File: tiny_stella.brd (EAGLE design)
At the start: 99.7 x 85.1 mm, 84 parts, among them IC1 74LS00D, SW1 RGT_DIFFICULTY, SW2 LFT_DIFFICULTY, SW3 ON/OFF, SW4 ON/OFF, T1 2N3904, T2 PN3906, T3 PN3906, T4 PN3906, X1 SSW-112-02-G-Q

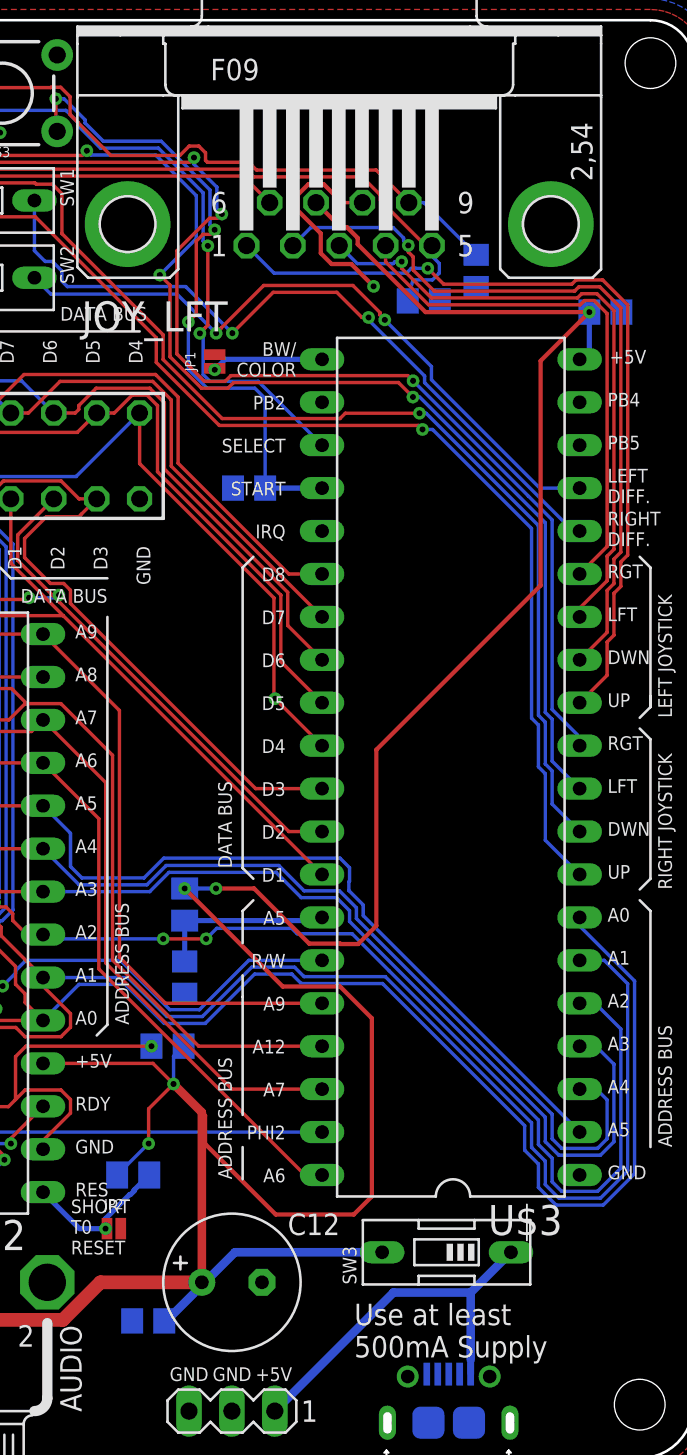
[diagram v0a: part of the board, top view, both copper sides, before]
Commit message: added monogram
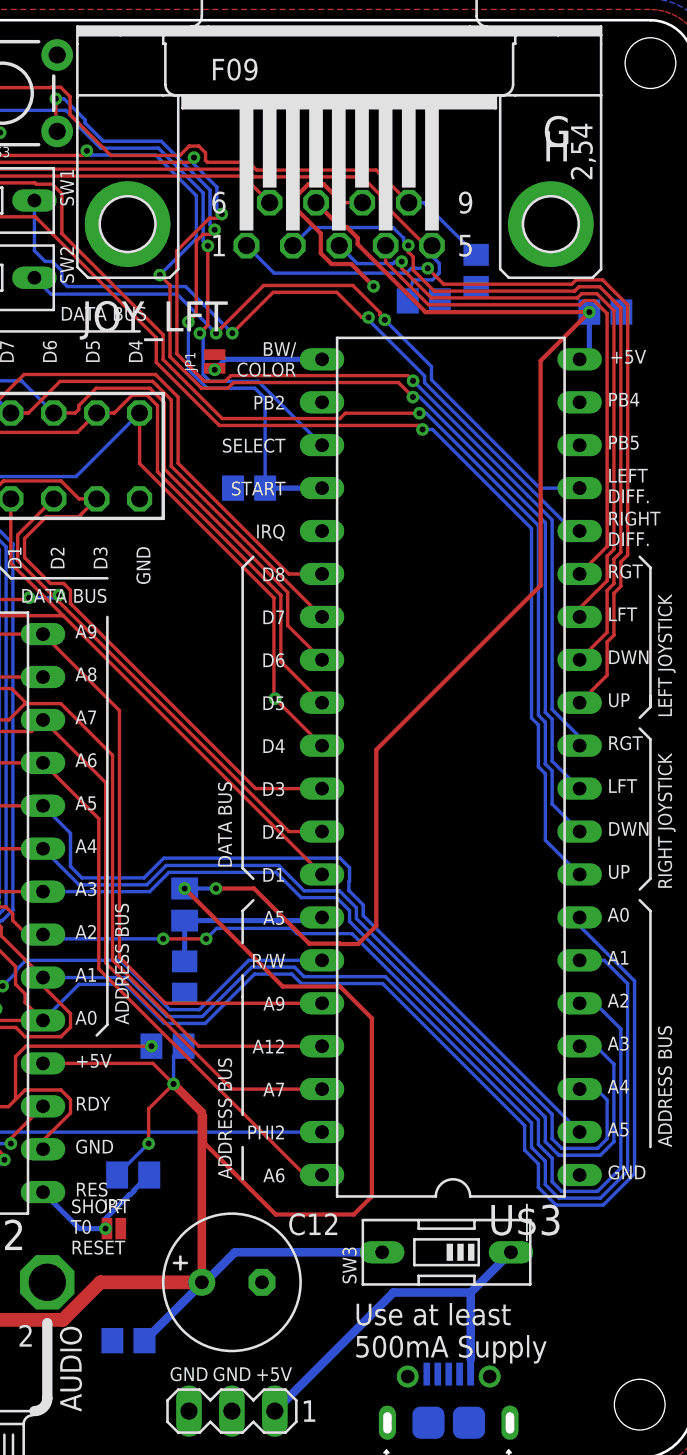
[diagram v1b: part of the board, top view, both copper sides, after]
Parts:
- moved C13 1.65 mm to (66.3, 6.96)
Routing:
- net +5V: track 466.9 -> 468.5 mm
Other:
- board text added: "G"
- board text added: "H"
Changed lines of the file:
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@@
 <dimension x1="99.695" y1="3.175" x2="0" y2="3.175" x3="49.8475" y3="-8.128" textsize="1.778" layer="48"/>
 <dimension x1="96.52" y1="0" x2="96.52" y2="85.09" x3="112.014" y3="42.545" textsize="1.778" layer="48"/>
+<text x="90.7796" y="77.6224" size="1.778" layer="25" font="vector">G</text>
+<text x="90.7796" y="76.7334" size="1.778" layer="25" font="vector">H</text>
 </plain>
 <attributes>
@@
 </element>
 <element name="C12" library="resistor" library_urn="urn:adsk.eagle:library:348" package="E3,5-8" package3d_urn="urn:adsk.eagle:package:25842/1" value="1F" x="72.39" y="10.414"/>
-<element name="C13" library="resistor" library_urn="urn:adsk.eagle:library:348" package="C0805" package3d_urn="urn:adsk.eagle:package:26137/1" value="100nF" x="67.437" y="8.128" smashed="yes" rot="MR0">
-<attribute name="NAME" x="70.358" y="9.271" size="0.8128" layer="26" rot="MR270"/>
-<attribute name="VALUE" x="68.707" y="5.588" size="1.27" layer="28" rot="MR0"/>
+<element name="C13" library="resistor" library_urn="urn:adsk.eagle:library:348" package="C0805" package3d_urn="urn:adsk.eagle:package:26137/1" value="100nF" x="66.2686" y="6.9596" smashed="yes" rot="MR0">
+<attribute name="NAME" x="69.1896" y="8.1026" size="0.8128" layer="26" rot="MR270"/>
+<attribute name="VALUE" x="67.5386" y="4.4196" size="1.27" layer="28" rot="MR0"/>
 </element>
 <element name="C14" library="resistor" library_urn="urn:adsk.eagle:library:348" package="C0805" package3d_urn="urn:adsk.eagle:package:26137/1" value="100nF" x="42.3164" y="68.8848" smashed="yes" rot="MR0">
@@
 <wire x1="27.625" y1="65.344" x2="33.02" y2="65.344" width="0.3048" layer="16"/>
 <wire x1="39.37" y1="46.675" x2="36.83" y2="46.675" width="0.3048" layer="16"/>
-<wire x1="68.387" y1="8.067" x2="68.387" y2="8.128" width="0.3048" layer="16"/>
-<wire x1="68.4149" y1="8.0391" x2="68.387" y2="8.067" width="0.3048" layer="16"/>
 <wire x1="70.7009" y1="10.3251" x2="70.612" y2="10.414" width="0.3048" layer="16"/>
 <wire x1="93.538" y1="67.818" x2="93.538" y2="65.598" width="0.3048" layer="16"/>
@@
 <wire x1="13.716" y1="29.874325" x2="13.716" y2="26.513675" width="0.254" layer="16"/>
 <wire x1="43.2664" y1="68.8848" x2="41.529" y2="67.1474" width="0.254" layer="16"/>
-<wire x1="70.7009" y1="10.3251" x2="68.4149" y2="8.0391" width="0.508" layer="16"/>
 <wire x1="77.3684" y1="74.295" x2="78.8162" y2="72.8472" width="0.254" layer="1"/>
 <wire x1="90.6554" y1="64.9354" x2="90.6554" y2="51.6438" width="0.254" layer="1"/>
@@
 <via x="71.4502" y="33.716" extent="1-16" drill="0.35"/>
 <wire x1="76.962" y1="30.4546" x2="73.7006" y2="33.716" width="0.254" layer="1"/>
+<wire x1="67.2186" y1="6.9596" x2="70.5841" y2="10.3251" width="0.508" layer="16"/>
+<wire x1="70.5841" y1="10.3251" x2="70.7009" y2="10.3251" width="0.508" layer="16"/>
 </signal>
 <signal name="N$6">

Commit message: silkscreen work
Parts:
- moved SW3 2.51 mm to (83.5, 10.3)
- renumbered U$1 to TIA, U$2 to 6507, U$3 to 6532
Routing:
- net +5V: track 468.5 -> 466.1 mm
- net VBUS: track 22.7 -> 20.4 mm

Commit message: yet more silkscreen
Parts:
- renumbered BRT_ADJ to BRIGHTNESS, SW1 to RDIFF, SW2 to LDIFF, SW3 to ON/OFF, SW4 to PAUSE
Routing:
- net +5V: track 466.1 -> 468.9 mm

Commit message: finished silkscreen, probably ready for manufacturing
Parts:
- moved R6 7.22 mm to (36.3, 22.4), turned to 180 degrees
- moved R1 3.21 mm to (32.8, 16.3), turned to 90 degrees
- moved C10 2.74 mm to (70.9, 56.4), turned to 270 degrees
- moved R15 2.50 mm to (2.03, 19.8), turned to 270 degrees
- moved R19 2.41 mm to (36.6, 19.1), turned to 90 degrees
- moved C3 2.27 mm to (35.8, 50.0)
- moved R26 2.27 mm to (38.4, 50.0)
- moved C11 2.27 mm to (38.4, 45.6)
- moved R12 2.27 mm to (35.8, 45.6)
- moved R2 1.83 mm to (33.3, 27.9), turned to 270 degrees
- moved R7 1.61 mm to (33.3, 23.9), turned to 90 degrees
- moved R18 1.44 mm to (67.6, 15.7), turned to 270 degrees
- moved R17 1.30 mm to (39.7, 19.1)
- moved C4 1.14 mm to (2.03, 23.9), turned to 270 degrees
- moved T4 0.76 mm to (40.0, 16.5)
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- renumbered BRIGHTNESS to BRIGHT, COLOR_ADJ to COLOR, JOY_RGT to RIGHT
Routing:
- net +5V: track 468.9 -> 443.3 mm, vias 19 -> 18
- net N$27: track 24.9 -> 14.4 mm, vias 2 -> 0
- net N$1: track 6.04 -> 14.0 mm, vias 0 -> 2
- net N$37: track 0.00 -> 5.39 mm, vias 0 -> 1
- net N$10: track 123.1 -> 125.9 mm
- net N$2: track 6.04 -> 8.39 mm, vias 0 -> 1
- net D8: track 92.4 -> 94.6 mm
- net D7: track 101.4 -> 103.5 mm
- net N$28: track 52.8 -> 51.2 mm
- net D4: track 110.3 -> 111.8 mm
- net D3: track 108.7 -> 109.9 mm
- net N$23: track 8.96 -> 7.83 mm
- net N$13: track 9.62 -> 10.5 mm
- net P_SW: track 93.3 -> 94.1 mm
- net N$8: track 28.3 -> 27.6 mm
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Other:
- board text added: "B/W"
- board text added: "LEFT PLAYER"
- board text added: "RESET"
- board text added: "RIGHT PLAYER"
- board text added: "SWITCHES"
- board text removed: "G"
- board text removed: "H"
- board text removed: "SHORT T0 RESET"
